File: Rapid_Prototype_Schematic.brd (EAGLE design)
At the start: 160 x 145.7 mm, 161 parts, among them IC2 SI4459ADY-T1-GE3, IC8 SI4485DY-T1-GE3, J1 XT60-M, J10 XT60-M, J2 XT60-M, J4 UJ2-MIBH-2-SMT-TR-67, J5 XT60-M, J6 XT60-M, J7 XT60-M, J8 XT60-M, J9 XT60-M, Q1 LTV-8141S, Q10 SI4435DDY, Q11 DMN65D8LFB-7, Q12 SI4435DDY, Q13 DMN65D8LFB-7, Q14 SI4435DDY, Q15 DMN65D8LFB-7, Q3 DMN65D8LFB-7, Q4 SI4435DDY, Q5 DMN65D8LFB-7, Q6 SI4435DDY, Q7 DMN65D8LFB-7, Q8 SI4435DDY, Q9 DMN65D8LFB-7, U1 LM35DM, U2 LM2904ITPX/NOPB, U3 LM2904ITPX/NOPB, U4 LM2904ITPX/NOPB, U5 LM2904ITPX/NOPB, U6 LM2904ITPX/NOPB, U7 TLV1117LV33DCYR, U8 LT1374IS8-5PBF

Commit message: Add files via upload
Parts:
- moved D1 226.5 mm to (94.0, 87.6), turned to 90 degrees
- moved SV1 208.5 mm to (119.4, 5.08)
- moved SV5 190.4 mm to (87.6, 29.2), turned to 90 degrees
- moved J2 168.2 mm to (118.1, 74.9)
- moved J1 152.2 mm to (118.1, 87.6)
- moved C21 136.6 mm to (106.7, 91.4)
- moved $2_3_$_2020-06-04_21-52-10 126.5 mm to (53.3, 66.0), turned to 180 degrees
- moved J9 44.9 mm to (-53.3, 47.0)
- moved TETHER 8.52 mm to (-128.3, -5.08)
- moved J10 6.84 mm to (-41.9, 72.4)
- moved D2 3.59 mm to (-16.5, 61.0)
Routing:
- net P_BATT+: track 0.00 -> 26.6 mm
- added copper zone on layer 1, net GND
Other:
- board size 160 x 145.7 mm -> 130 x 95 mm

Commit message: Placed Parts
Added Connectors for the Port side on the Board Layout
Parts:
- moved J8 238.9 mm to (118.1, 52.1), turned to 180 degrees
- moved J6 203.2 mm to (118.1, 61.0), turned to 180 degrees
- moved J5 185.6 mm to (118.1, 69.8), turned to 180 degrees
- moved Q14 168.9 mm to (99.1, 61.0), turned to 270 degrees
- moved Q6 146.0 mm to (99.1, 52.1), turned to 270 degrees
- moved J7 14.0 mm to (-104.1, 47.0)
- moved J9 11.7 mm to (-41.9, 49.5)
- moved J10 11.4 mm to (-41.9, 61.0)
- moved J2 3.81 mm to (118.1, 78.7), turned to 180 degrees
- turned J1 to 180 degrees
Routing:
- net P_BATT+: track 26.6 -> 17.3 mm

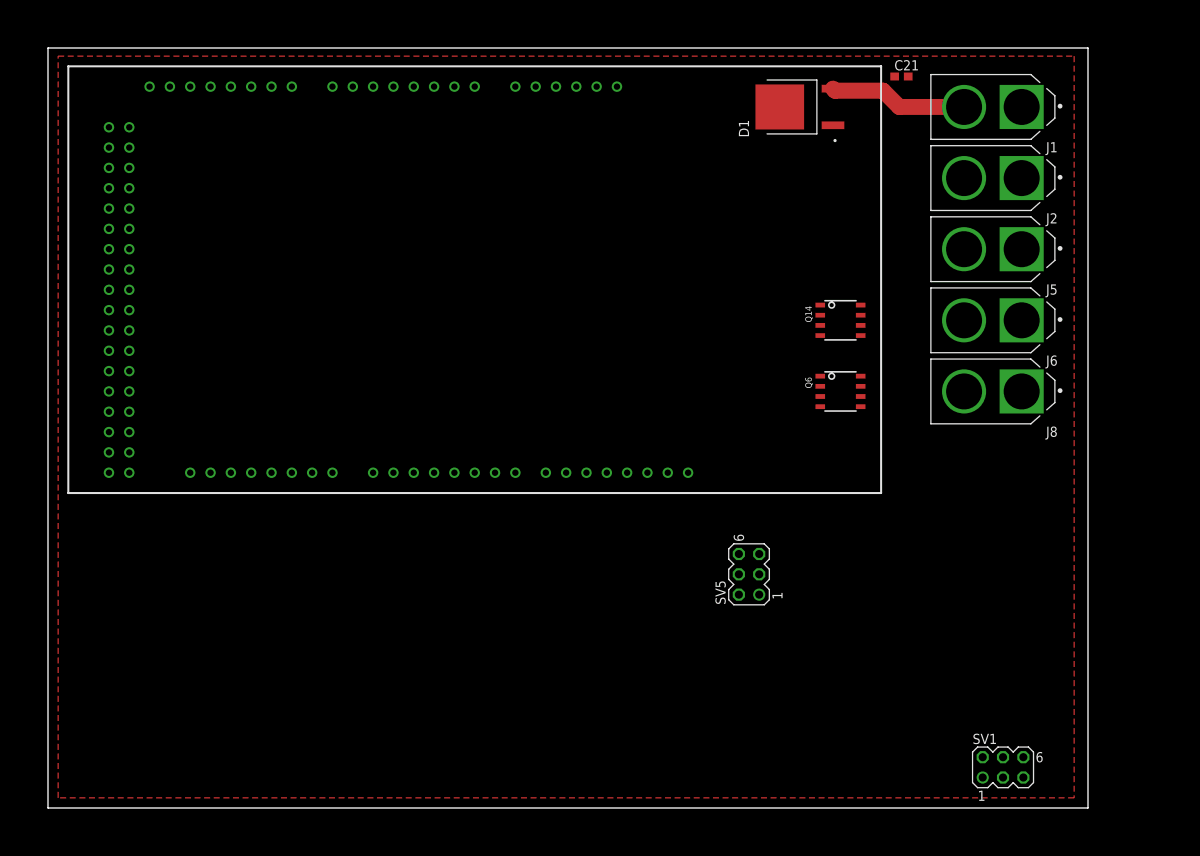
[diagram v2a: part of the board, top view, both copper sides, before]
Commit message: Update Rapid_Prototype_Schematic.brd
Adjusted width for the Board Layout
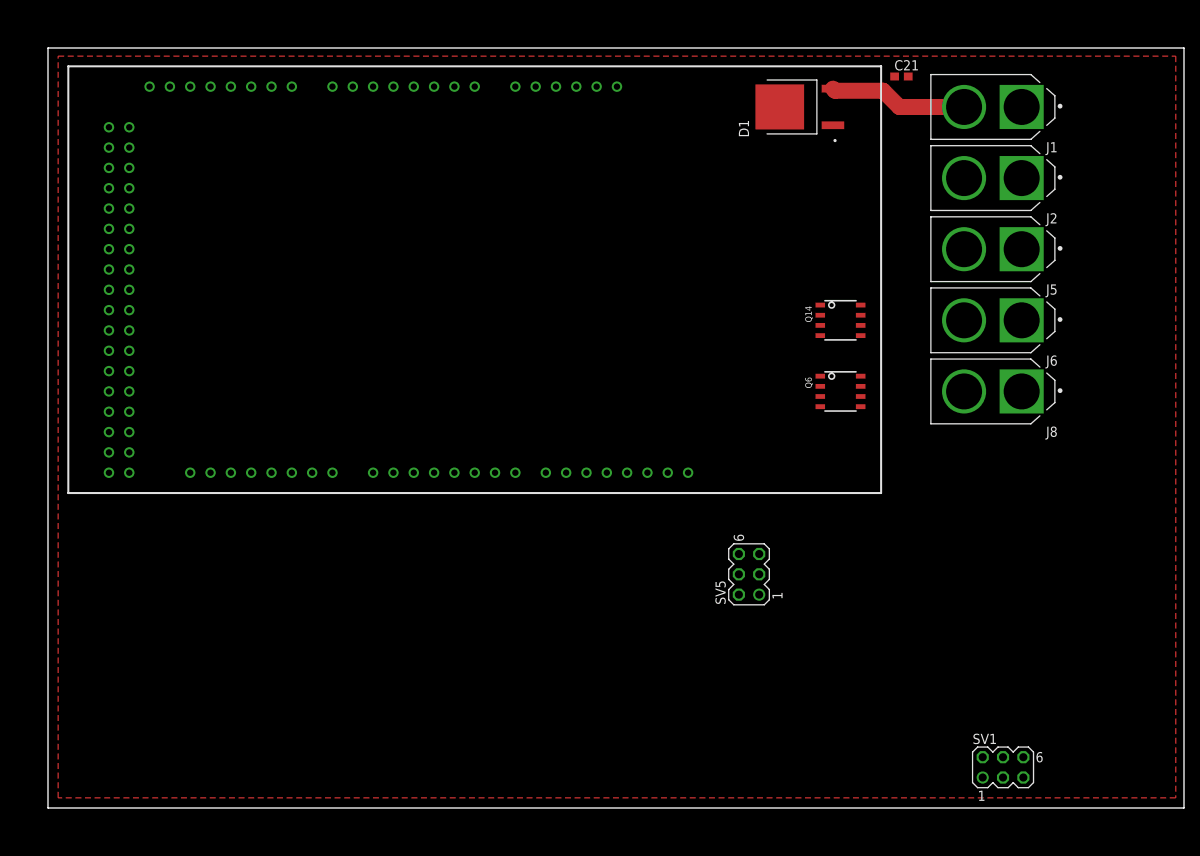
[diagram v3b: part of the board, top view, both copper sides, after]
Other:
- board size 130 x 95 mm -> 142 x 95 mm
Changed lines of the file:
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@@
 <board>
 <plain>
-<wire x1="0" y1="0" x2="130" y2="0" width="0" layer="20"/>
-<wire x1="130" y1="0" x2="130" y2="95" width="0" layer="20"/>
-<wire x1="130" y1="95" x2="0" y2="95" width="0" layer="20"/>
+<wire x1="0" y1="0" x2="142" y2="0" width="0" layer="20"/>
+<wire x1="142" y1="0" x2="142" y2="95" width="0" layer="20"/>
+<wire x1="142" y1="95" x2="0" y2="95" width="0" layer="20"/>
 <wire x1="0" y1="95" x2="0" y2="0" width="0" layer="20"/>
 </plain>
@@
 <polygon width="0.25" layer="1">
 <vertex x="1.27" y="93.98"/>
-<vertex x="128.27" y="93.98"/>
-<vertex x="128.27" y="1.27"/>
+<vertex x="140.97" y="93.98"/>
+<vertex x="140.97" y="1.27"/>
 <vertex x="1.27" y="1.27"/>
 </polygon>

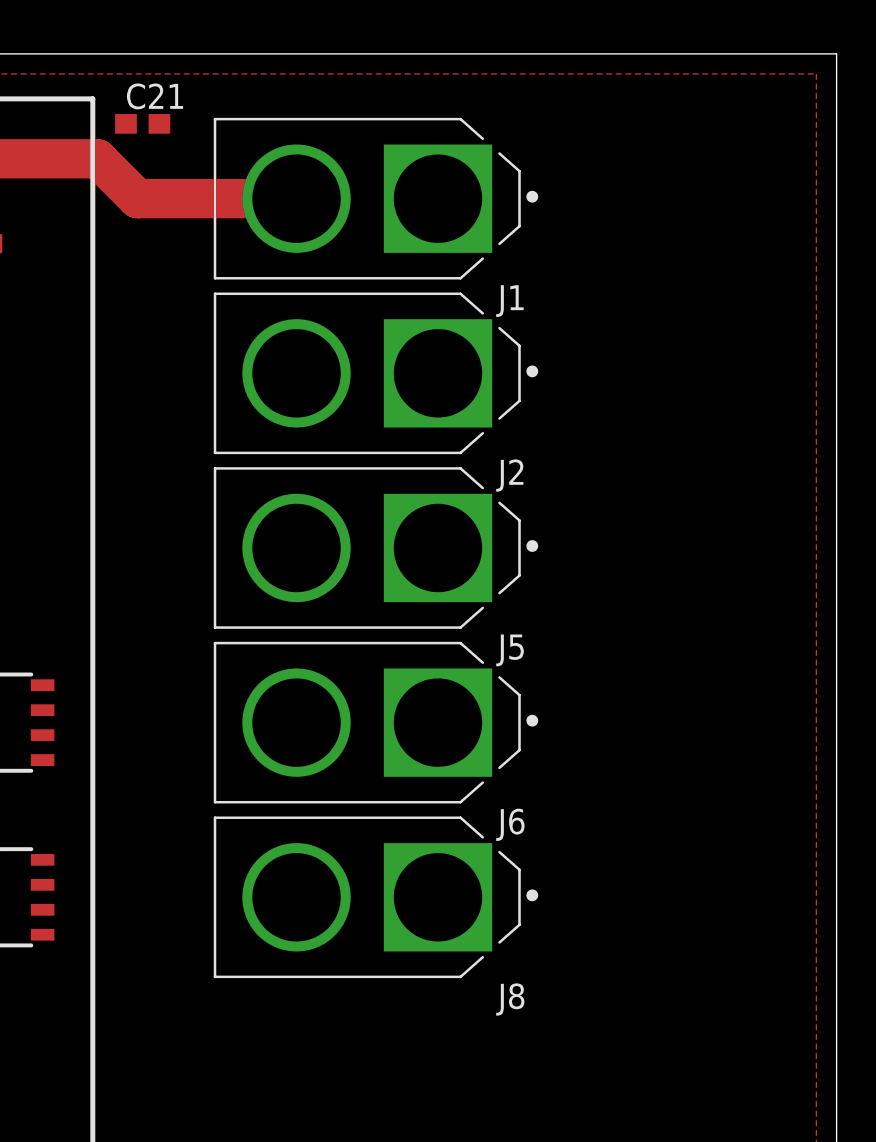
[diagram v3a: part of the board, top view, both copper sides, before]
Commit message: Update Rapid_Prototype_Schematic.brd
Changed Power circuit positions
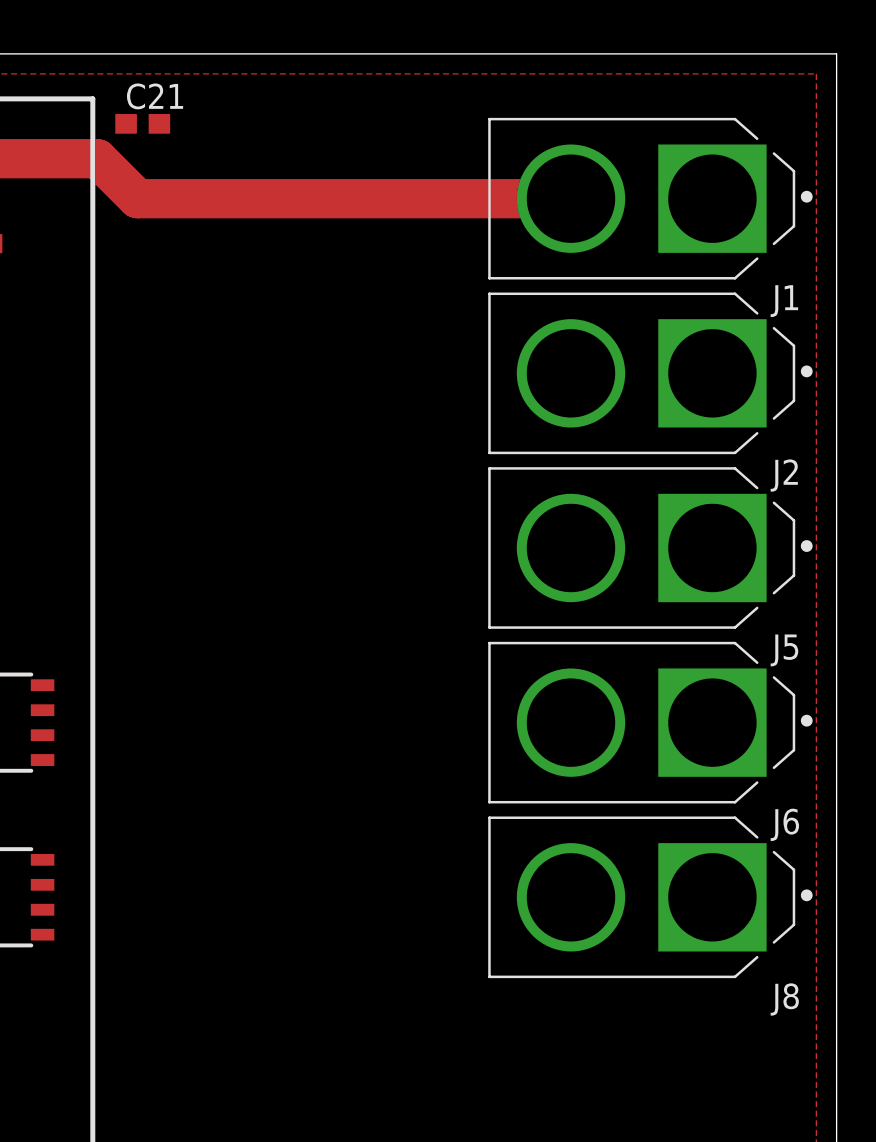
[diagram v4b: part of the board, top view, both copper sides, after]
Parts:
- moved J1 14.0 mm to (132.1, 87.6)
- moved J2 14.0 mm to (132.1, 78.7)
- moved J5 14.0 mm to (132.1, 69.8)
- moved J6 14.0 mm to (132.1, 61.0)
- moved J8 14.0 mm to (132.1, 52.1)
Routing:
- net P_BATT+: track 17.3 -> 31.3 mm

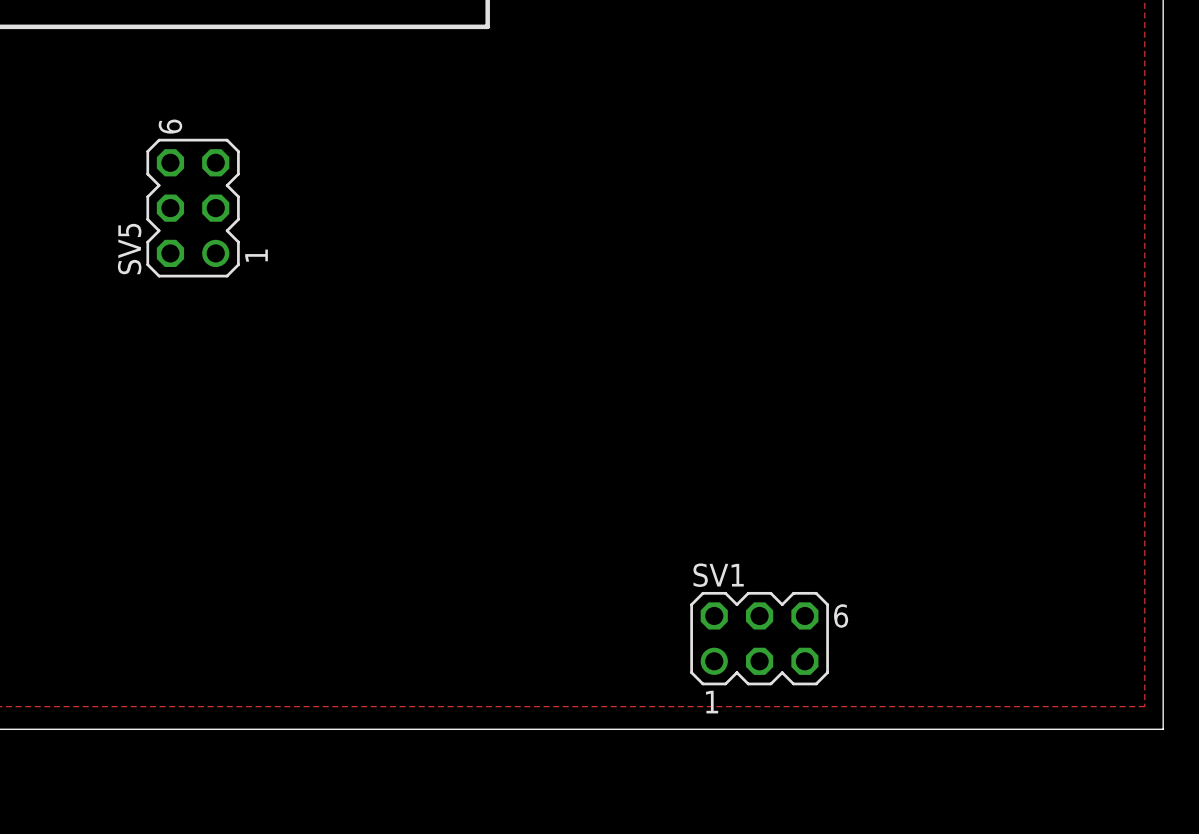
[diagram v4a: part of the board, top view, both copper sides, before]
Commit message: Tenda Custom Device
Created a custom Tenda device that can be modified later to fit the measurements implemented from mechanical.
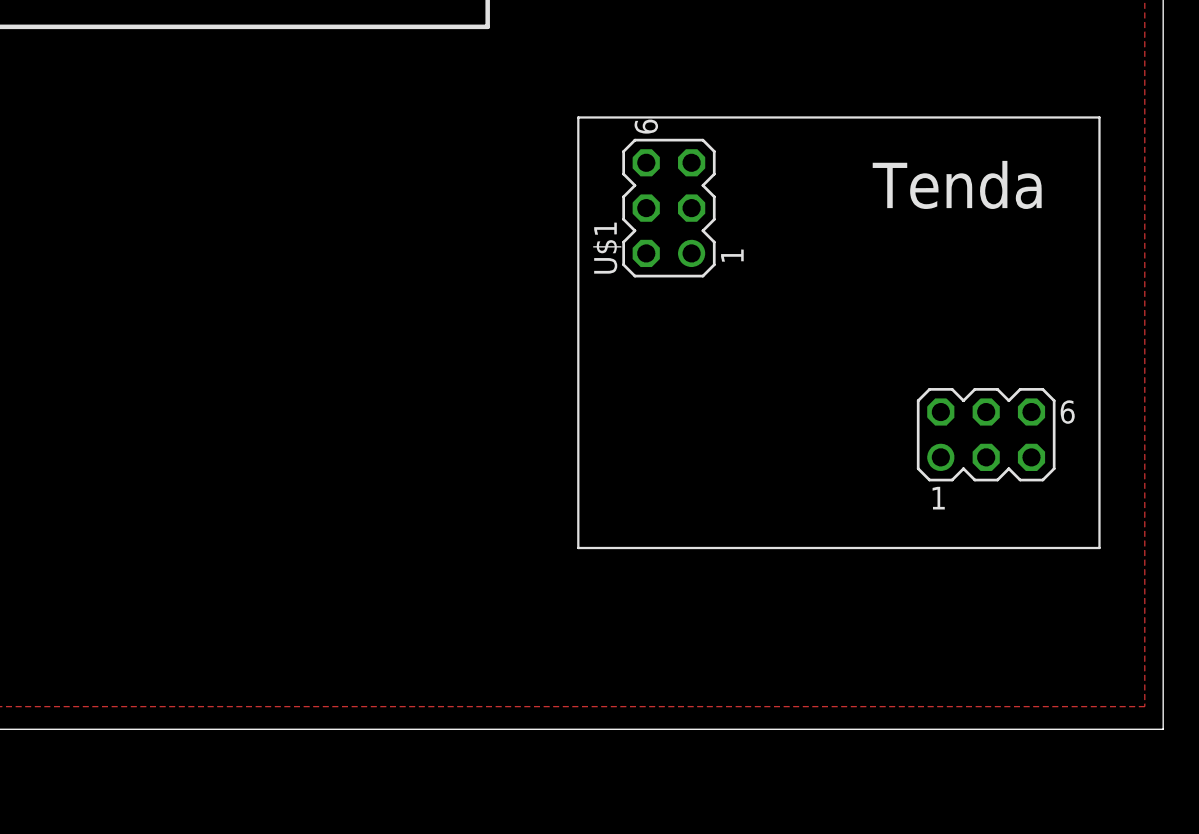
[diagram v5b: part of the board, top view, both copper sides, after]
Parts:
- removed SV1: J1, con-lstb:MA03-2
- removed SV5: J5, con-lstb:MA03-2
- added U$1: TENDA, tenda:TENDA
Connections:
- net +3V3: now also U$1.11, U$1.12; no longer SV5.5, SV5.6
- net GND: now also U$1.7; no longer SV5.1
- net N$53: now also U$1.10; no longer SV5.4
- net N$55: now also U$1.8; no longer SV5.2
- net N$57: now also U$1.9; no longer SV5.3
- net TETHER_A: now also U$1.1, U$1.2; no longer SV1.1, SV1.2
- net TETHER_B: now also U$1.5, U$1.6; no longer SV1.5, SV1.6

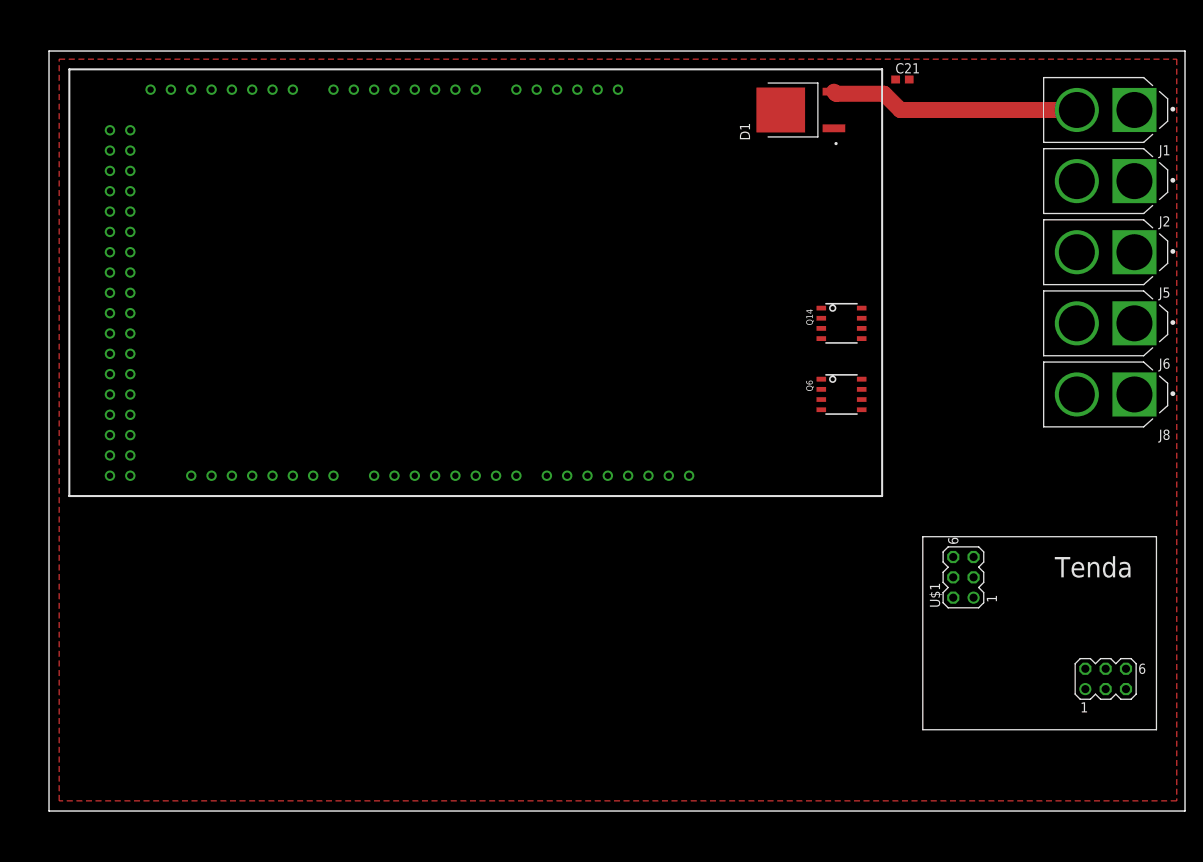
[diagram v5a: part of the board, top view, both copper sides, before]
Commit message: Tenda Header Measurements
Tenda Header Measurements implemented
Fixed positions of the ground pours and the arduino mega
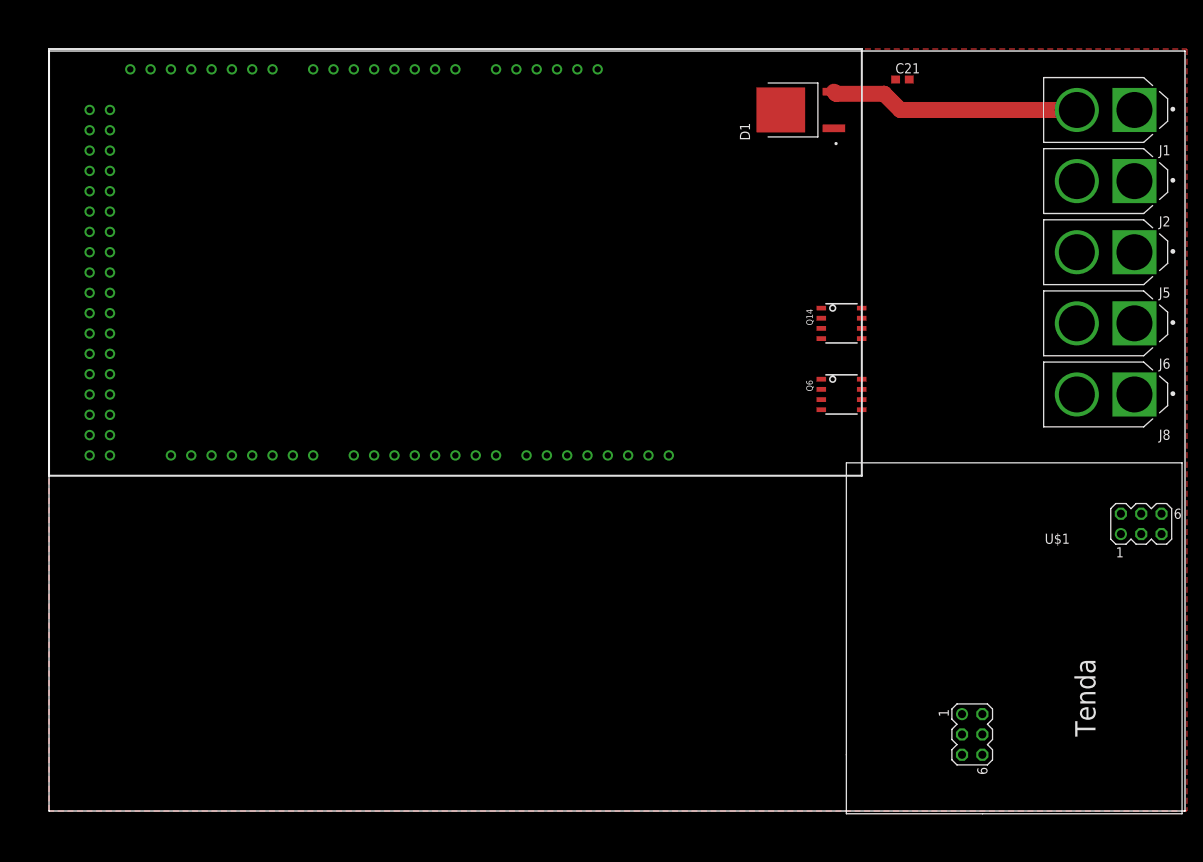
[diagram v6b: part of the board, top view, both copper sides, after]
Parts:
- moved $2_3_$_2020-06-04_21-52-10 3.59 mm to (50.8, 68.6)
- moved U$1 2.54 mm to (120.7, 21.6), turned to 270 degrees
